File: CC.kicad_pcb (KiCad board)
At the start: 2 copper layers, 74.5 x 34 mm, 46 parts, among them J1 BAT, J3 Conn_02x20_Counter_Clockwise, Q1 Q_DUAL_NPN, SW1 SW-2P, U1 CH9328, U2 CP2102N-A01-GQFN28, U3 ESP32-WROOM-32D, U4 AMS1117-3.3, U5 BL1530-DPDT

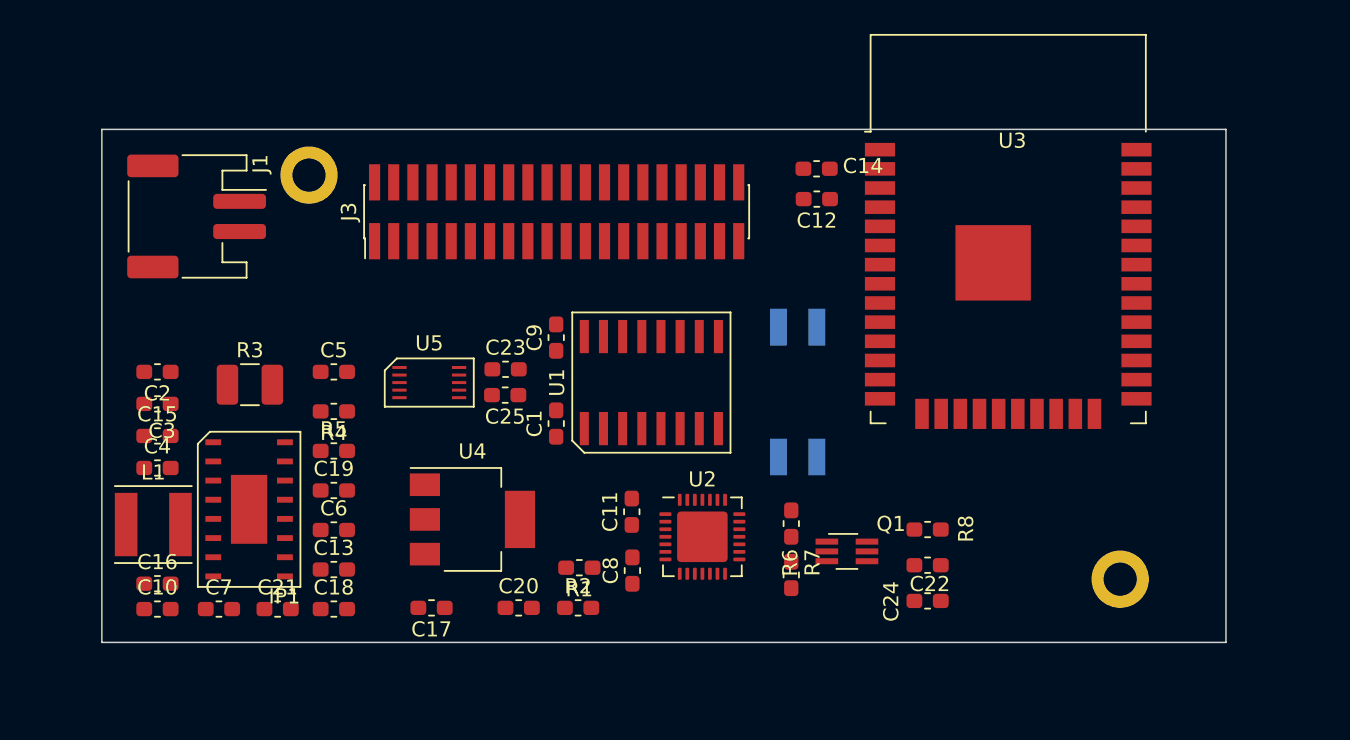
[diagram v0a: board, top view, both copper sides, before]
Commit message: feat: update the pin socket to 2.54 mm
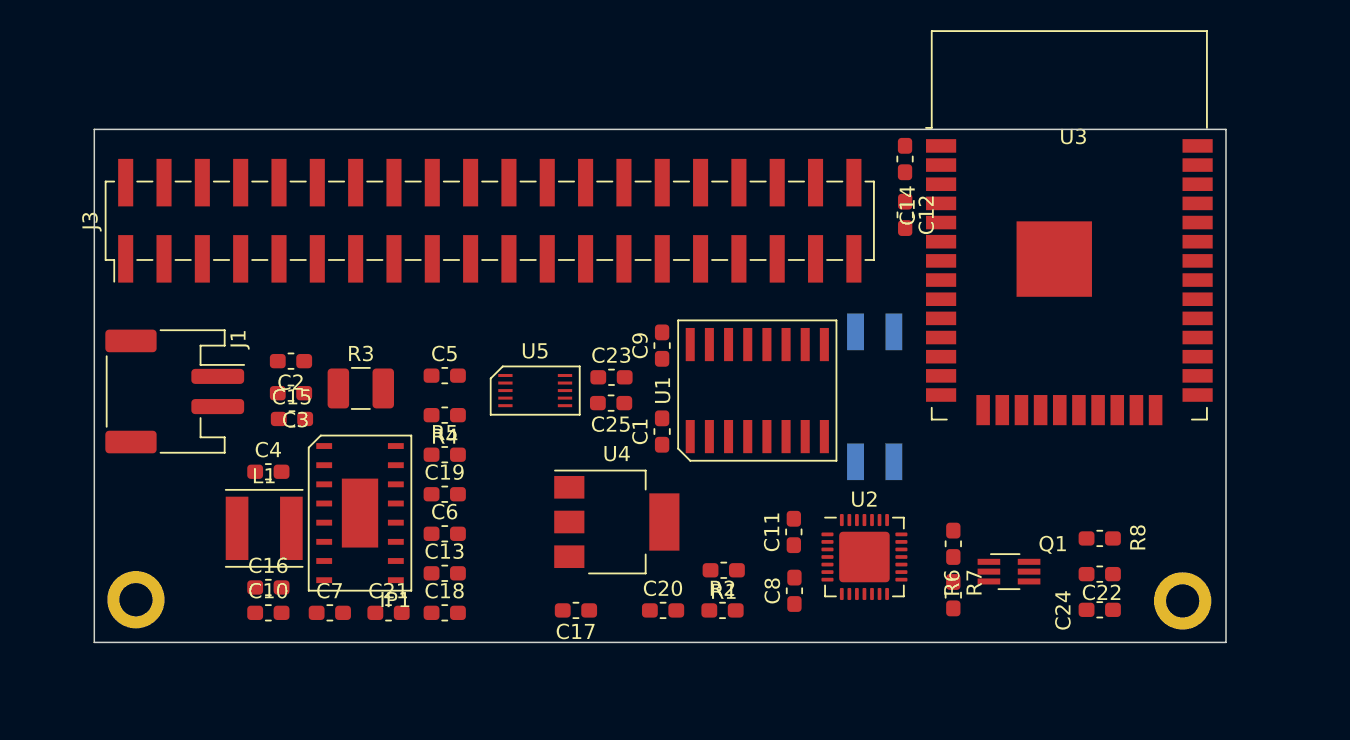
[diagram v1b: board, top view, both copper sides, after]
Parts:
- J3: footprint Connector_PinHeader_1.27mm:PinHeader_2x20_P1.27mm_Vertical_SMD -> Connector_PinHeader_2.54mm:PinHeader_2x20_P2.54mm_Vertical_SMD
- moved H1 30.4 mm to (32.8, 51.2)
- moved J1 11.7 mm to (35.3, 37.4)
- moved C22 11.4 mm to (96.6, 49.5)
- moved C24 11.4 mm to (96.6, 51.8)
- moved R8 11.4 mm to (96.6, 47.1)
- moved C8 10.8 mm to (76.4, 50.6)
- moved Q1 10.8 mm to (90.6, 49.3)
- moved R6 10.8 mm to (86.9, 47.5)
- moved R7 10.8 mm to (86.9, 50.9)
- moved U2 10.8 mm to (81.0, 48.3)
- moved C11 10.8 mm to (76.4, 46.7)
- moved R2 9.57 mm to (71.6, 51.9)
- moved C17 9.57 mm to (61.9, 51.9)
- moved R1 9.57 mm to (71.7, 49.2)
- moved C20 9.57 mm to (67.7, 51.9)
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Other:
- board size 74.5 x 34 mm -> 75 x 34 mm

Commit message: fix: fix the pinsocket and pinheader config
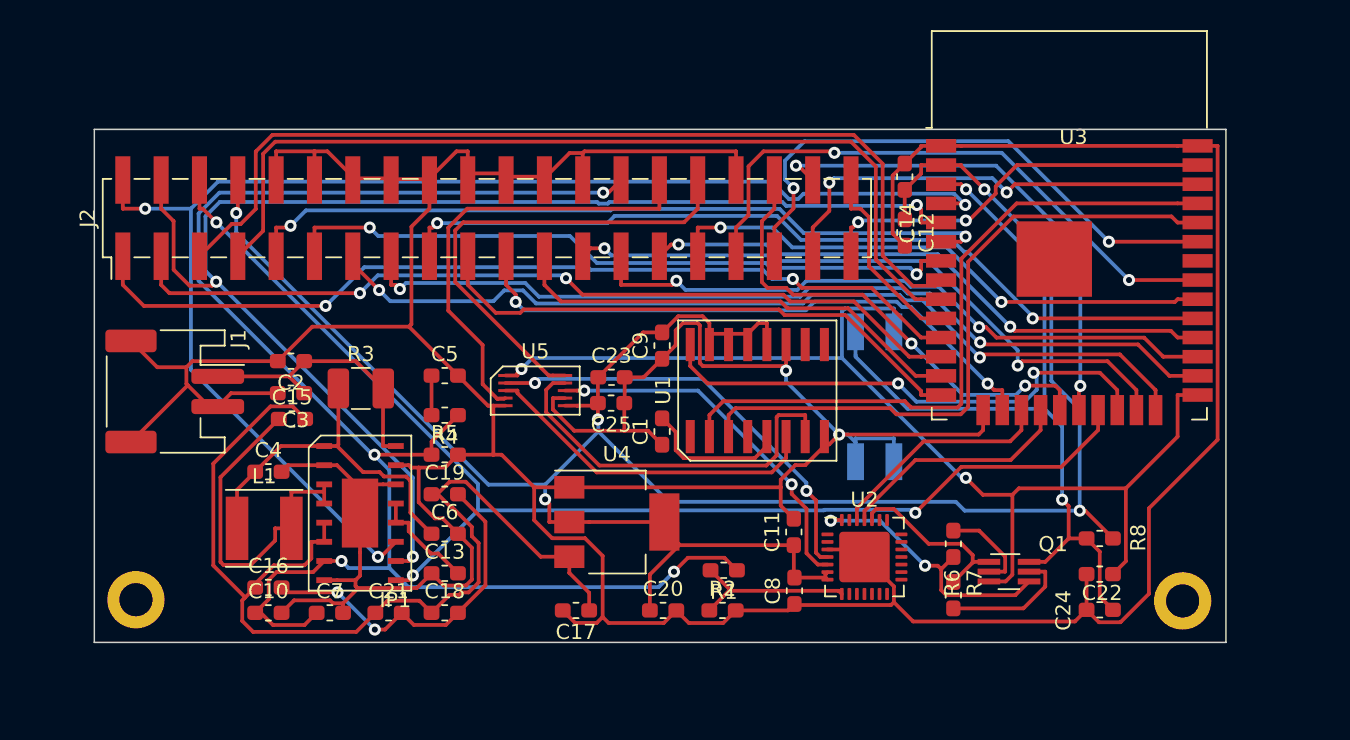
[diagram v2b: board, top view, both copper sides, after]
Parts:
- removed J3: Conn_02x20_Counter_Clockwise, Connector_PinHeader_2.54mm:PinHeader_2x20_P2.54mm_Vertical_SMD
- added J2: Conn_02x20_Odd_Even, Connector_PinHeader_2.54mm:PinHeader_2x20_P2.54mm_Vertical_SMD, F.Cu at (56.0, 25.9)
- moved C14 1.17 mm to (83.7, 23.1)
- moved C12 1.17 mm to (83.7, 26.8)
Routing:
- net GND: track 0.00 -> 352.4 mm, vias 0 -> 2
- net VDD33: track 0.00 -> 159.1 mm, vias 0 -> 5
- net VBUS: track 0.00 -> 105.5 mm, vias 0 -> 4
- net /L3: track 0.00 -> 90.9 mm, vias 0 -> 3
- net /L2: track 0.00 -> 89.6 mm, vias 0 -> 3
- net /L1: track 0.00 -> 81.8 mm, vias 0 -> 3
- net /IO0: track 0.00 -> 75.8 mm, vias 0 -> 2
- net VDD5V: track 0.00 -> 68.9 mm
- net /ROW3: track 0.00 -> 62.6 mm
- net /ROW4: track 0.00 -> 60.7 mm
- net /COL1: track 0.00 -> 59.7 mm, vias 0 -> 2
- net /ROW1: track 0.00 -> 59.7 mm, vias 0 -> 2
- net /COL2: track 0.00 -> 58.7 mm, vias 0 -> 2
- net /ROW2: track 0.00 -> 56.5 mm, vias 0 -> 2
- net /COL3: track 0.00 -> 56.0 mm, vias 0 -> 2
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
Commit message: feat: change the 2 pin connector from jst ph to jst xh
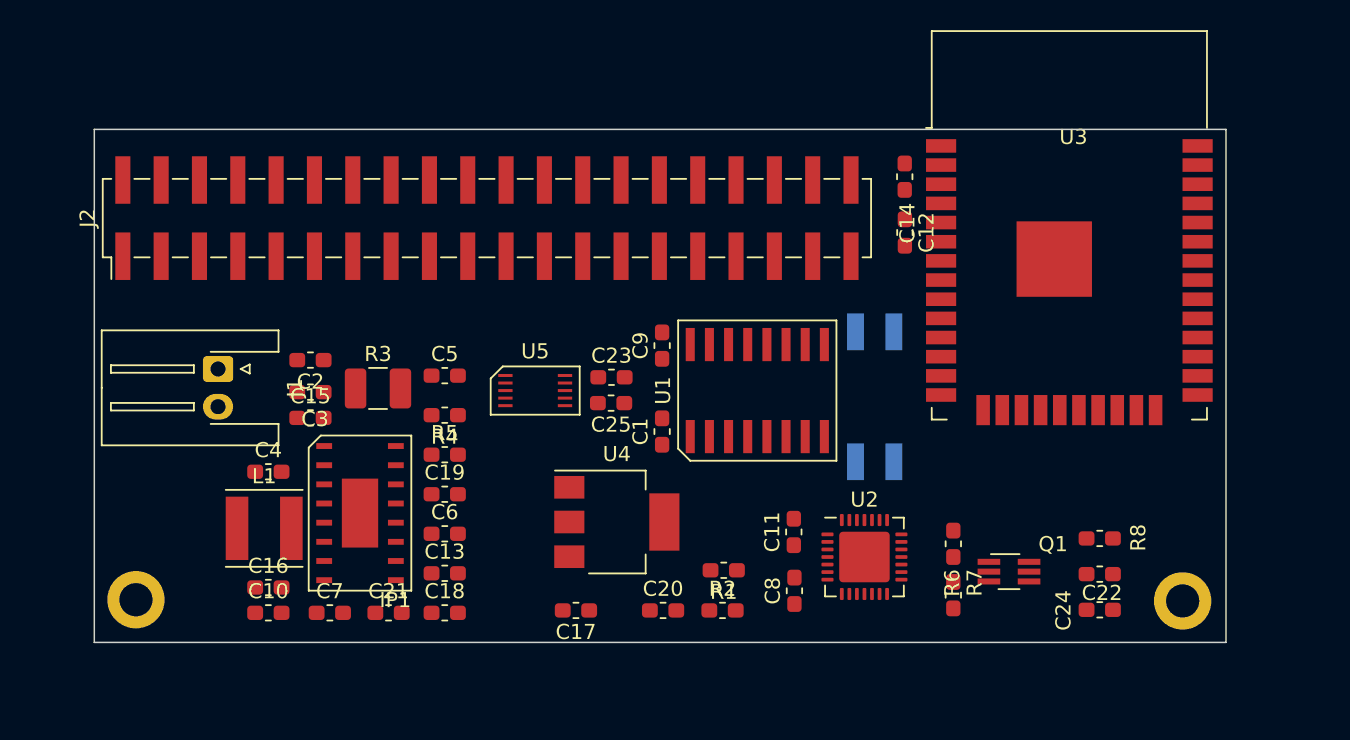
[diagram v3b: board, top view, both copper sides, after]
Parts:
- J1: value BAT -> Conn_01x02_Female; footprint Connector_JST:JST_PH_S2B-PH-SM4-TB_1x02-1MP_P2.00mm_Horizontal -> Connector_JST:JST_XH_S2B-XH-A-1_1x02_P2.50mm_Horizontal
- moved J1 3.23 mm to (38.2, 35.9)
- moved C2 1.29 mm to (44.3, 35.3)
- moved C3 1.29 mm to (44.3, 37.4)
- moved C15 1.23 mm to (44.3, 39.1)
- moved R3 1.14 mm to (48.8, 37.2)
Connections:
- J1 pad 1: +BATT -> GND
- J1 pad 2: GND -> +BATT
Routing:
- net GND: track 352.4 -> 0.00 mm, vias 2 -> 0
- net VDD33: track 159.1 -> 0.00 mm, vias 5 -> 0
- net VBUS: track 105.5 -> 0.00 mm, vias 4 -> 0
- net /L3: track 90.9 -> 0.00 mm, vias 3 -> 0
- net /L2: track 89.6 -> 0.00 mm, vias 3 -> 0
- net /L1: track 81.8 -> 0.00 mm, vias 3 -> 0
- net /IO0: track 75.8 -> 0.00 mm, vias 2 -> 0
- net VDD5V: track 68.9 -> 0.00 mm
- net /ROW3: track 62.6 -> 0.00 mm
- net /ROW4: track 60.7 -> 0.00 mm
- net /COL1: track 59.7 -> 0.00 mm, vias 2 -> 0
- net /ROW1: track 59.7 -> 0.00 mm, vias 2 -> 0
- net /COL2: track 58.7 -> 0.00 mm, vias 2 -> 0
- net /ROW2: track 56.5 -> 0.00 mm, vias 2 -> 0
- net /COL3: track 56.0 -> 0.00 mm, vias 2 -> 0
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
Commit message: feat: update the jst package
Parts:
- J1: footprint Connector_JST:JST_XH_S2B-XH-A-1_1x02_P2.50mm_Horizontal -> keyboard:JST_XH_S2B-XH-A-1_1x02_P2.50mm_Horizontal
- moved C2 1.29 mm to (43.0, 35.4)
- moved C3 1.29 mm to (43.0, 37.5)
- moved C15 1.23 mm to (43.1, 39.2)
- moved R3 1.14 mm to (47.7, 37.2)
- moved J1 0.92 mm to (38.9, 35.3)
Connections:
- U3 pad 39: (no net) -> GND

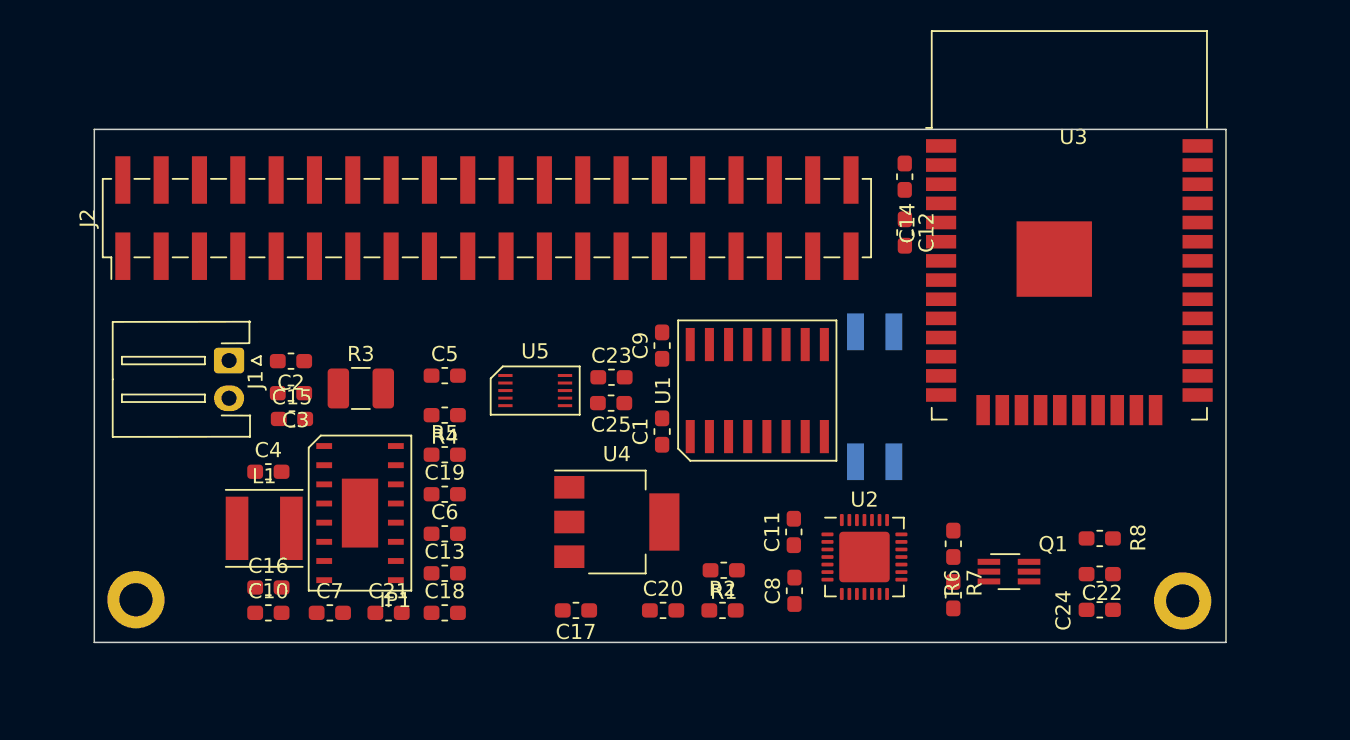
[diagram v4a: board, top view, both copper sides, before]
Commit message: feat: rerouting the cc and keyboard
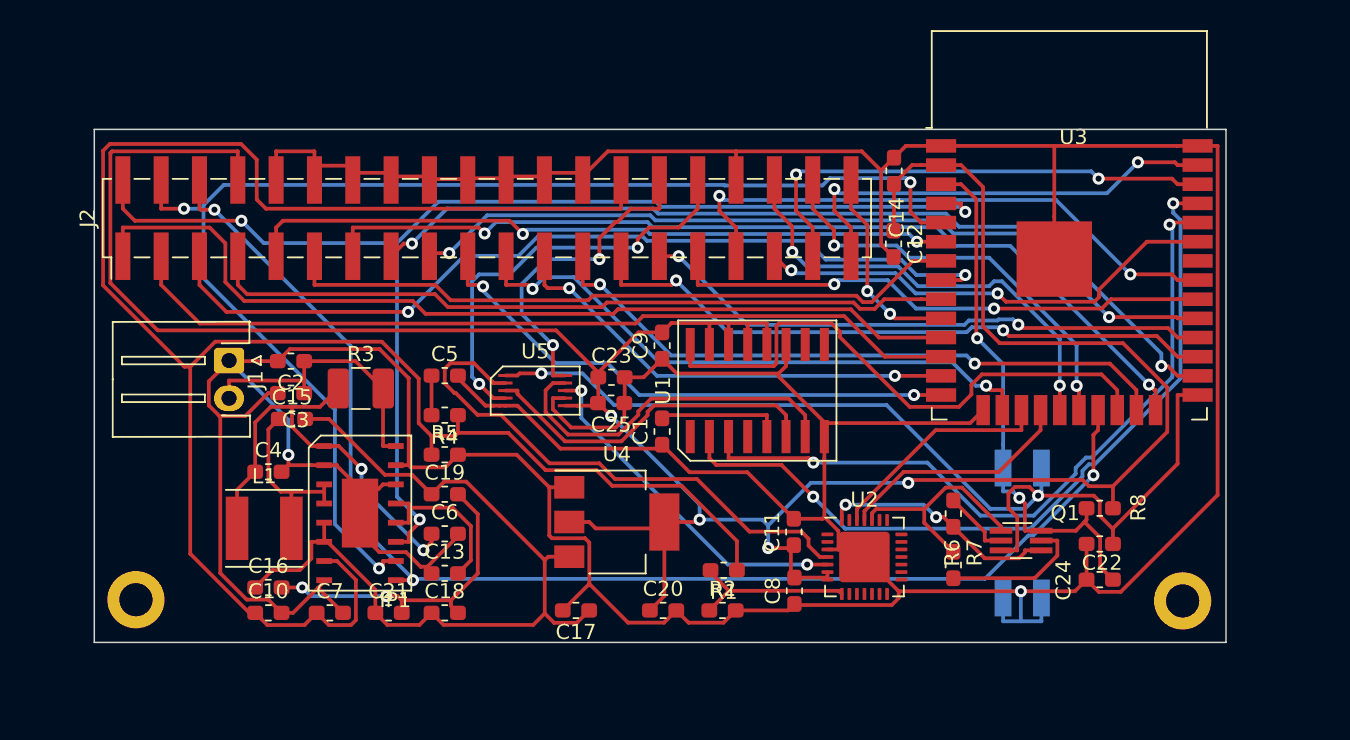
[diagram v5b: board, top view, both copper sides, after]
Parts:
- moved SW1 13.3 mm to (91.5, 46.8)
- moved Q1 2.21 mm to (91.4, 47.2)
- moved C22 2.00 mm to (96.6, 47.5)
- moved C24 2.00 mm to (96.6, 49.8)
- moved R6 2.00 mm to (86.9, 45.5)
- moved R7 2.00 mm to (86.9, 48.9)
- moved R8 2.00 mm to (96.6, 45.1)
- moved C12 1.06 mm to (83.0, 27.6)
- moved C14 0.81 mm to (83.0, 22.8)
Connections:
- J2 pad 30: /USBD_P -> /USBD_N
- J2 pad 32: /USBD_N -> /USBD_P
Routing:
- net GND: track 0.00 -> 351.6 mm, vias 0 -> 2
- net VDD33: track 0.00 -> 181.8 mm, vias 0 -> 4
- net VBUS: track 0.00 -> 136.7 mm
- net /L2: track 0.00 -> 87.1 mm, vias 0 -> 3
- net /L1: track 0.00 -> 86.4 mm, vias 0 -> 3
- net /L3: track 0.00 -> 83.7 mm, vias 0 -> 3
- net /IO0: track 0.00 -> 68.2 mm, vias 0 -> 2
- net /COL1: track 0.00 -> 61.5 mm, vias 0 -> 2
- net /ROW1: track 0.00 -> 60.9 mm
- net /COL2: track 0.00 -> 59.8 mm, vias 0 -> 2
- net /ROW3: track 0.00 -> 58.3 mm, vias 0 -> 2
- net /ROW2: track 0.00 -> 56.0 mm
- net VDD5V: track 0.00 -> 55.8 mm
- net /COL3: track 0.00 -> 54.9 mm, vias 0 -> 2
- net /KTXD: track 0.00 -> 52.3 mm, vias 0 -> 2
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
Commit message: feat: update the routing for the differential pair
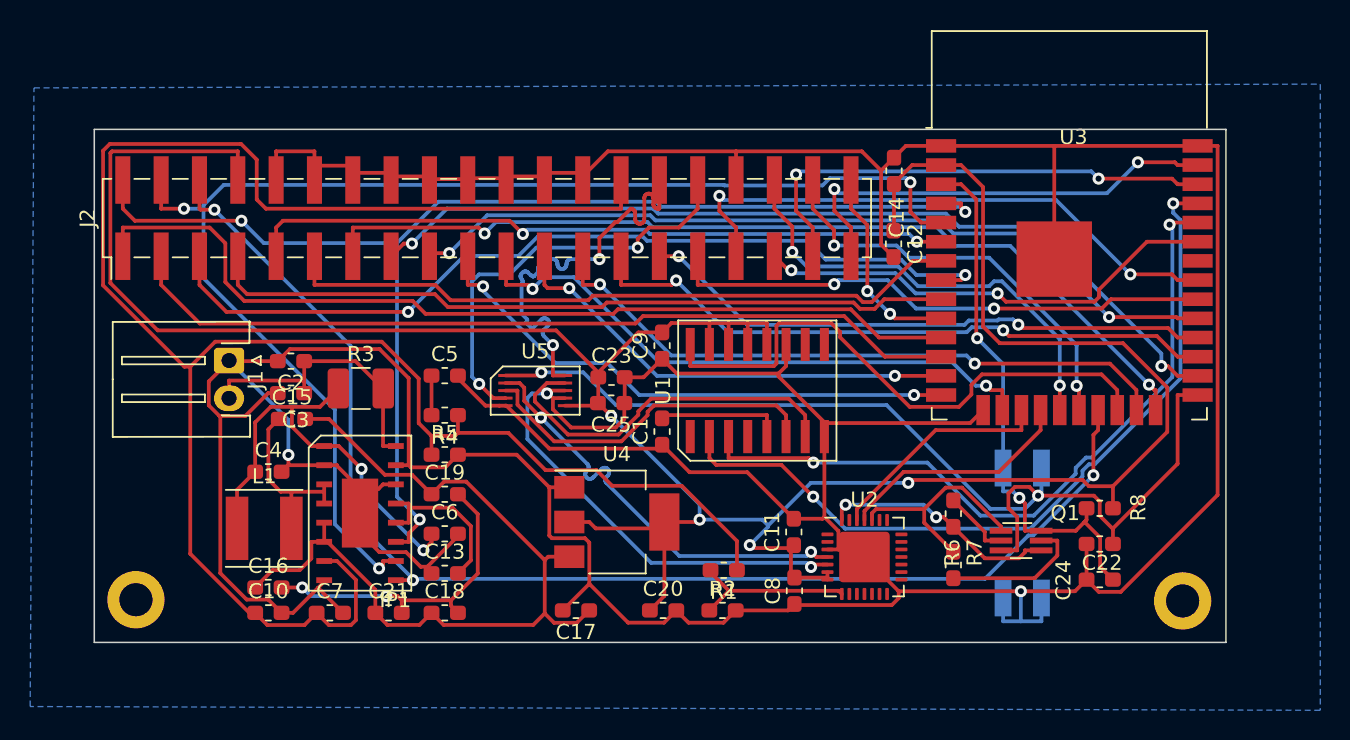
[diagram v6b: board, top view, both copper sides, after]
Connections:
- net /FD_N renamed /FD-
- net /FD_P renamed /FD+
- net /KD_N renamed /KD-
- net /KD_P renamed /KD+
- net /USBD_N renamed /USBD-
- net /USBD_P renamed /USBD+
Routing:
- net /FD+: track 36.1 -> 28.9 mm, vias 0 -> 2
- net /USBD-: track 21.6 -> 28.4 mm
- net /FD-: track 23.2 -> 28.9 mm
- net VDD33: track 181.8 -> 183.4 mm
- net /KD-: track 23.7 -> 24.6 mm
- added copper zone on B.Cu, net GND
